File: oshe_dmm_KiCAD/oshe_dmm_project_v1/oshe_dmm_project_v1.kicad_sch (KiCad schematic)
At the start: 46 parts, among them J1 FTDI Basic, J2 USB_C_Receptacle_PowerOnly_6P, J3 Conn_01x02, SW1 SW_Push, U1 ATmega328P-A, U2 INA219BxD, U3 BQ24075RGT, U4 LM317_SOT-223, Y1 16MHz

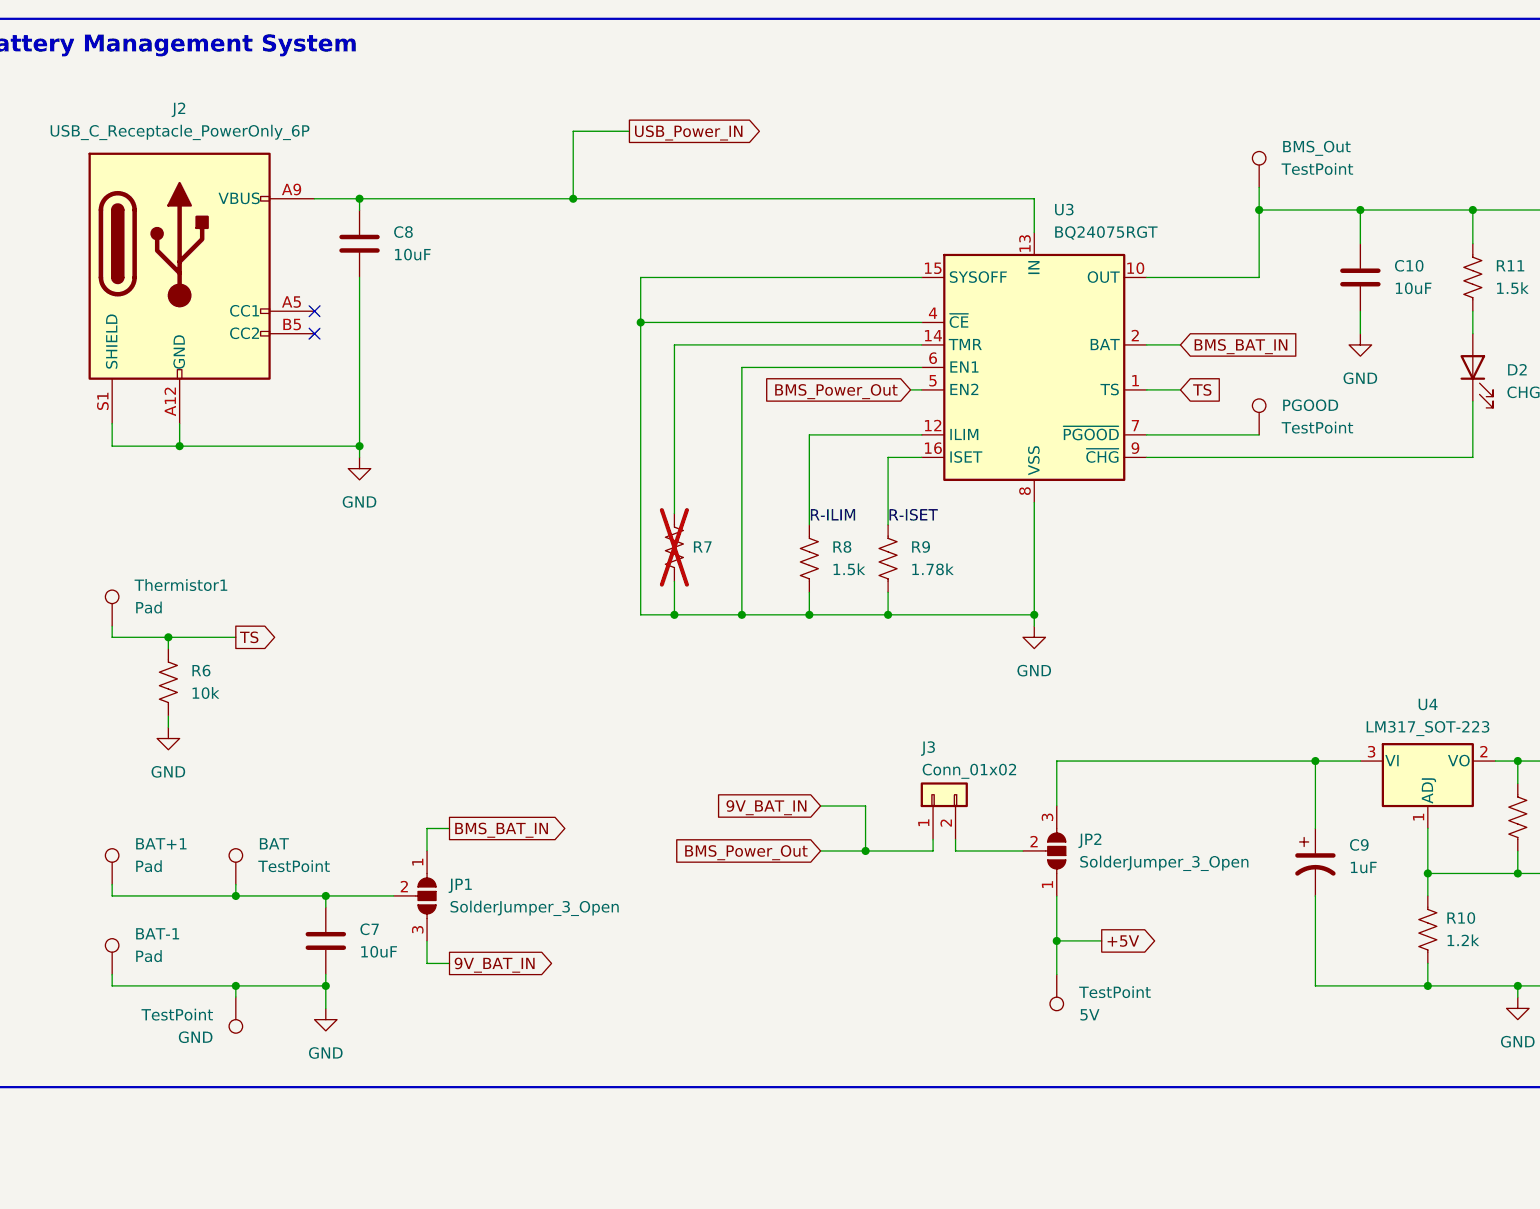
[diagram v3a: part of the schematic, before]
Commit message: Finalized the BMS system
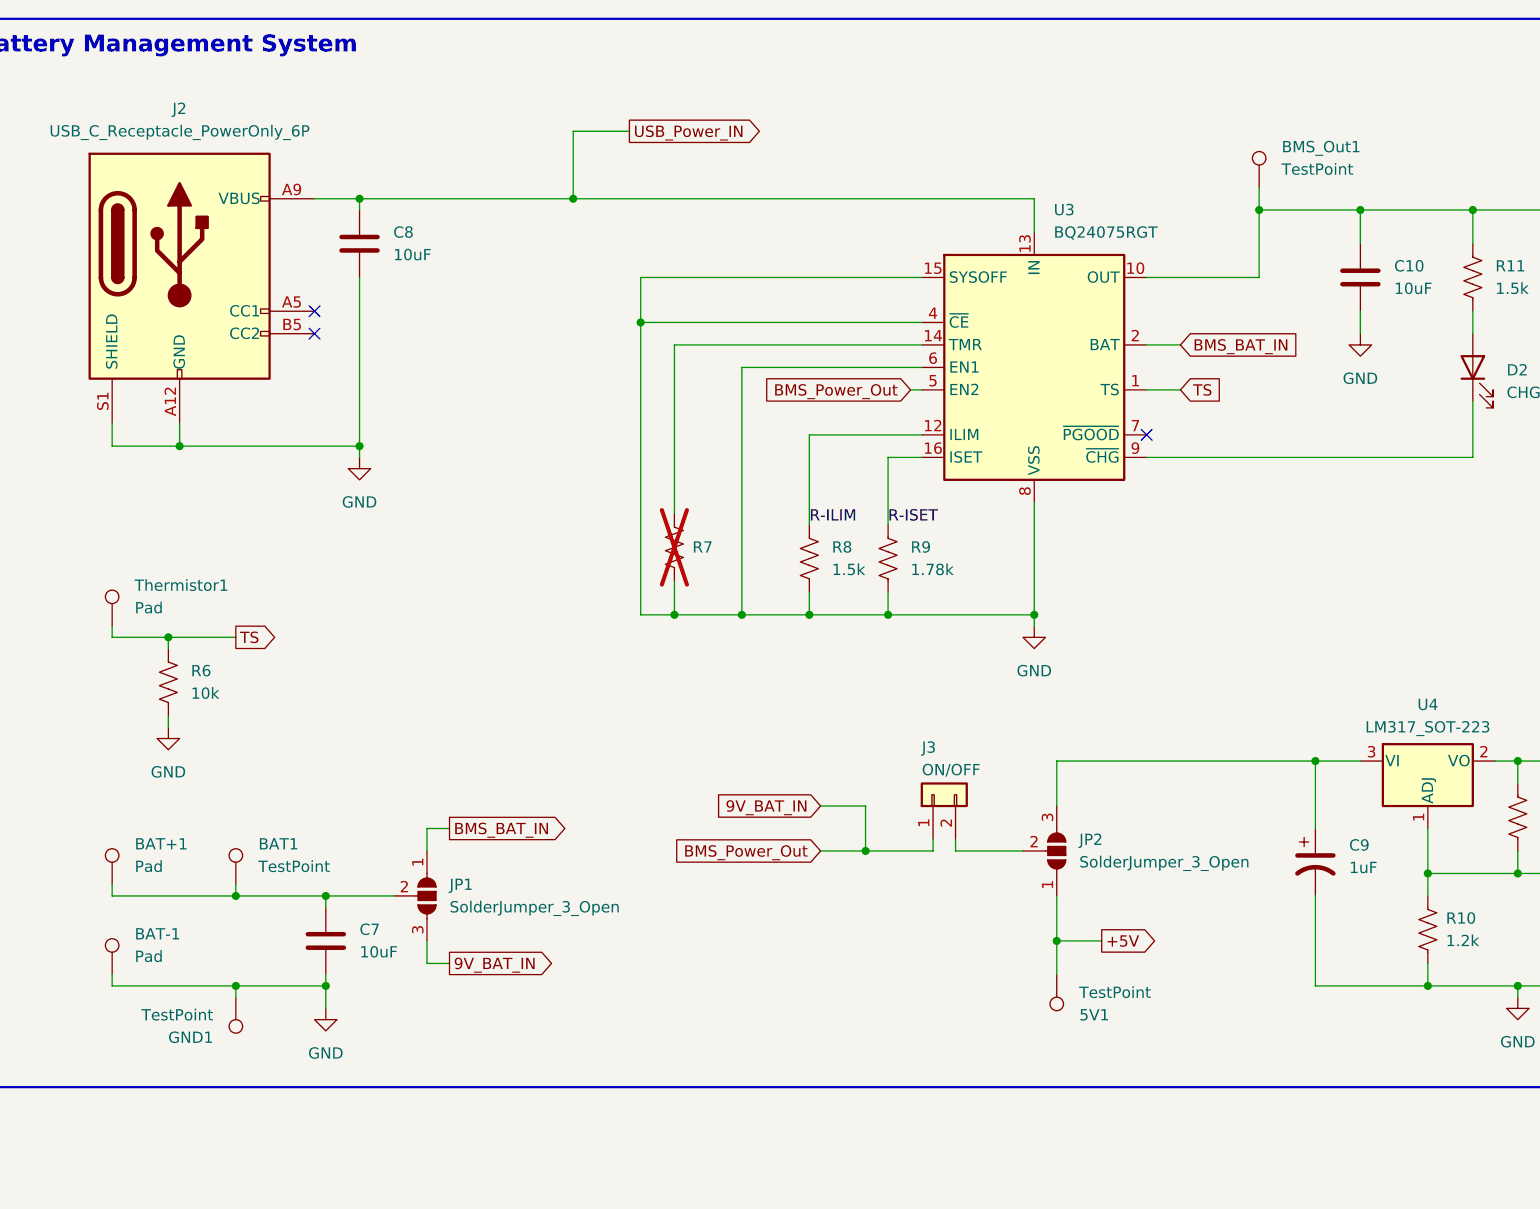
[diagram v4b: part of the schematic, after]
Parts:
- removed PGOOD: TestPoint, TestPoint:TestPoint_Keystone_5019_Minature, symbol Connector:TestPoint
- J3: value Conn_01x02 -> ON/OFF
- renumbered 5V to 5V1, BAT to BAT1, BMS_Out to BMS_Out1, GND to GND1
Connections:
- no-connect marks 2 -> 3
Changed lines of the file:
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@@
 	)
 	(no_connect
+		(at 490.22 63.5)
+	)
+	(no_connect
 		(at 396.24 52.07)
 	)
@@
 	(wire
 		(pts
-			(xy 490.22 63.5) (xy 502.92 63.5)
-		)
-		(stroke
-			(width 0)
-			(type default)
-		)
-	)
-	(wire
-		(pts
 			(xy 509.27 125.73) (xy 521.97 125.73)
 		)
@@
 		(dnp no)
 		(fields_autoplaced yes)
-		(property "Reference" "#PWR09"
+		(property "Reference" "#PWR011"
 			(at 401.32 72.39 0)
 			(effects
@@
 			(project "oshe_dmm_project_v1"
 				(path "/24c8480a-c336-4df0-8536-7016ee8fc0ac"
-					(reference "#PWR09")
+					(reference "#PWR011")
 					(unit 1)
 				)
@@
 		(on_board yes)
 		(dnp no)
-		(property "Reference" "BAT"
+		(property "Reference" "BAT1"
 			(at 389.89 109.7279 0)
 			(effects
@@
 			(project "oshe_dmm_project_v1"
 				(path "/24c8480a-c336-4df0-8536-7016ee8fc0ac"
-					(reference "BAT")
+					(reference "BAT1")
 					(unit 1)
 				)
@@
 		(on_board yes)
 		(dnp no)
-		(property "Reference" "5V"
+		(property "Reference" "5V1"
 			(at 482.6 129.0321 0)
 			(effects
@@
 			(project "oshe_dmm_project_v1"
 				(path "/24c8480a-c336-4df0-8536-7016ee8fc0ac"
-					(reference "5V")
+					(reference "5V1")
 					(unit 1)
 				)
@@
 		(dnp no)
 		(fields_autoplaced yes)
-		(property "Reference" "#PWR05"
+		(property "Reference" "#PWR07"
 			(at 111.76 72.39 0)
 			(effects
@@
 			(project ""
 				(path "/24c8480a-c336-4df0-8536-7016ee8fc0ac"
-					(reference "#PWR05")
+					(reference "#PWR07")
 					(unit 1)
 				)
@@
 		(dnp no)
 		(fields_autoplaced yes)
-		(property "Reference" "#PWR08"
+		(property "Reference" "#PWR010"
 			(at 397.51 134.62 0)
 			(effects
@@
 			(project "oshe_dmm_project_v1"
 				(path "/24c8480a-c336-4df0-8536-7016ee8fc0ac"
-					(reference "#PWR08")
+					(reference "#PWR010")
 					(unit 1)
 				)
@@
 		(dnp no)
 		(fields_autoplaced yes)
-		(property "Reference" "#PWR015"
+		(property "Reference" "#PWR04"
 			(at 67.31 180.34 0)
 			(effects
@@
 			(project "oshe_dmm_project_v1"
 				(path "/24c8480a-c336-4df0-8536-7016ee8fc0ac"
-					(reference "#PWR015")
+					(reference "#PWR04")
 					(unit 1)
 				)
@@
 	)
 	(symbol
-		(lib_id "Connector:TestPoint")
-		(at 502.92 63.5 0)
-		(unit 1)
-		(exclude_from_sim no)
-		(in_bom yes)
-		(on_board yes)
-		(dnp no)
-		(property "Reference" "PGOOD"
-			(at 505.46 60.198 0)
-			(effects
-				(font
-					(size 1.27 1.27)
-				)
-				(justify left)
-			)
-		)
-		(property "Value" "TestPoint"
-			(at 505.46 62.738 0)
-			(effects
-				(font
-					(size 1.27 1.27)
-				)
-				(justify left)
-			)
-		)
-		(property "Footprint" "TestPoint:TestPoint_Keystone_5019_Minature"
-			(at 508 63.5 0)
-			(effects
-				(font
-					(size 1.27 1.27)
-				)
-				(hide yes)
-			)
-		)
-		(property "Datasheet" "~"
-			(at 508 63.5 0)
-			(effects
-				(font
-					(size 1.27 1.27)
-				)
-				(hide yes)
-			)
-		)
-		(property "Description" "test point"
-			(at 502.92 63.5 0)
-			(effects
-				(font
-					(size 1.27 1.27)
-				)
-				(hide yes)
-			)
-		)
-		(pin "1"
-		)
-		(instances
-			(project ""
-				(path "/24c8480a-c336-4df0-8536-7016ee8fc0ac"
-					(reference "PGOOD")
-					(unit 1)
-				)
-			)
-		)
-	)
-	(symbol
 		(lib_id "Switch:SW_Push")
 		(at 90.17 86.36 90)
@@
 		(dnp no)
 		(fields_autoplaced yes)
-		(property "Reference" "#PWR010"
+		(property "Reference" "#PWR012"
 			(at 477.52 91.44 0)
 			(effects
@@
 			(project "oshe_dmm_project_v1"
 				(path "/24c8480a-c336-4df0-8536-7016ee8fc0ac"
-					(reference "#PWR010")
+					(reference "#PWR012")
 					(unit 1)
 				)
@@
 		(on_board yes)
 		(dnp no)
-		(property "Reference" "GND"
+		(property "Reference" "GND1"
 			(at 384.81 131.5721 0)
 			(effects
@@
 			(project "oshe_dmm_project_v1"
 				(path "/24c8480a-c336-4df0-8536-7016ee8fc0ac"
-					(reference "GND")
+					(reference "GND1")
 					(unit 1)
 				)
@@
 		(dnp no)
 		(fields_autoplaced yes)
-		(property "Reference" "#PWR03"
+		(property "Reference" "#PWR05"
 			(at 77.47 38.1 0)
 			(effects
@@
 			(project "oshe_dmm_project_v1"
 				(path "/24c8480a-c336-4df0-8536-7016ee8fc0ac"
-					(reference "#PWR03")
+					(reference "#PWR05")
 					(unit 1)
 				)
@@
 		(dnp no)
 		(fields_autoplaced yes)
-		(property "Reference" "#PWR04"
+		(property "Reference" "#PWR06"
 			(at 90.17 99.06 0)
 			(effects
@@
 			(project "oshe_dmm_project_v1"
 				(path "/24c8480a-c336-4df0-8536-7016ee8fc0ac"
-					(reference "#PWR04")
+					(reference "#PWR06")
 					(unit 1)
 				)
@@
 			)
 		)
-		(property "Value" "Conn_01x02"
+		(property "Value" "ON/OFF"
 			(at 464.82 101.346 90)
 			(effects
@@
 		(dnp no)
 		(fields_autoplaced yes)
-		(property "Reference" "#PWR07"
+		(property "Reference" "#PWR09"
 			(at 379.73 102.87 0)
 			(effects
@@
 			(project "oshe_dmm_project_v1"
 				(path "/24c8480a-c336-4df0-8536-7016ee8fc0ac"
-					(reference "#PWR07")
+					(reference "#PWR09")
 					(unit 1)
 				)
@@
 		(on_board yes)
 		(dnp no)
-		(property "Reference" "BMS_Out"
+		(property "Reference" "BMS_Out1"
 			(at 505.46 30.9879 0)
 			(effects
@@
 			(project "oshe_dmm_project_v1"
 				(path "/24c8480a-c336-4df0-8536-7016ee8fc0ac"
-					(reference "BMS_Out")
+					(reference "BMS_Out1")
 					(unit 1)
 				)
@@
 		(dnp no)
 		(fields_autoplaced yes)
-		(property "Reference" "#PWR02"
+		(property "Reference" "#PWR03"
 			(at 58.42 120.65 0)
 			(effects
@@
 			(project "oshe_dmm_project_v1"
 				(path "/24c8480a-c336-4df0-8536-7016ee8fc0ac"
-					(reference "#PWR02")
+					(reference "#PWR03")
 					(unit 1)
 				)
@@
 		(dnp no)
 		(fields_autoplaced yes)
-		(property "Reference" "#PWR06"
+		(property "Reference" "#PWR08"
 			(at 118.11 46.99 0)
 			(effects
@@
 			(project "oshe_dmm_project_v1"
 				(path "/24c8480a-c336-4df0-8536-7016ee8fc0ac"
-					(reference "#PWR06")
+					(reference "#PWR08")
 					(unit 1)
 				)
@@
 		(on_board yes)
 		(dnp no)
-		(property "Reference" "#PWR013"
+		(property "Reference" "#PWR02"
 			(at 53.34 152.4 0)
 			(effects
@@
 			(project "oshe_dmm_project_v1"
 				(path "/24c8480a-c336-4df0-8536-7016ee8fc0ac"
-					(reference "#PWR013")
+					(reference "#PWR02")
 					(unit 1)
 				)
@@
 		(dnp no)
 		(fields_autoplaced yes)
-		(property "Reference" "#PWR012"
+		(property "Reference" "#PWR014"
 			(at 532.13 133.35 0)
 			(effects
@@
 			(project "oshe_dmm_project_v1"
 				(path "/24c8480a-c336-4df0-8536-7016ee8fc0ac"
-					(reference "#PWR012")
+					(reference "#PWR014")
 					(unit 1)
 				)
@@
 		(dnp no)
 		(fields_autoplaced yes)
-		(property "Reference" "#PWR011"
+		(property "Reference" "#PWR013"
 			(at 514.35 58.42 0)
 			(effects
@@
 			(project "oshe_dmm_project_v1"
 				(path "/24c8480a-c336-4df0-8536-7016ee8fc0ac"
-					(reference "#PWR011")
+					(reference "#PWR013")
 					(unit 1)
 				)

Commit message: Made some PCB and Schematic Changes
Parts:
- added C4: 0.15 μf, oshe:CKG57K, symbol Device:C
- added COMin1, Vin1: ~, symbol oshe:Input
- added D1: SMAJ200CA, Diode_SMD:D_SMA, symbol Diode:SMAJ200CA
- added F1: Fuse, Fuse:Fuseholder_Clip-5x20mm_Keystone_3512P_Inline_P23.62x7.27mm_D1.02x2.41x1.02x1.57mm_Horizontal, symbol Device:Fuse
- added J4: Conn_01x16, Connector_PinSocket_2.54mm:PinSocket_1x16_P2.54mm_Vertical, symbol Connector_Generic:Conn_01x16
- added R1: R_US, Resistor_SMD:R_1206_3216Metric_Pad1.30x1.75mm_HandSolder, symbol Device:R_US
- added R15: 900K, symbol Device:R
- added R16: 90k, symbol Device:R
- added R17: 9k, symbol Device:R
- added R18: 1k, symbol Device:R
- added R4: 10k, Resistor_SMD:R_1206_3216Metric_Pad1.30x1.75mm_HandSolder, symbol Device:R_US
- added RV1: Varistor, symbol Device:Varistor
- added RV2: 10k, Potentiometer_SMD:Potentiometer_ACP_CA6-VSMD_Vertical, symbol Device:R_Potentiometer_US
- added SW2: SW_Rotary_1x4_MP, symbol Switch:SW_Rotary_1x4_MP
- added TP1: V-, symbol Connector:TestPoint_Probe
- added TP2: V+, symbol Connector:TestPoint_Probe
- added U5: ADS1115IDGS, Package_SO:TSSOP-10_3x3mm_P0.5mm, symbol Analog_ADC:ADS1115IDGS
- added Vout+1, Vout-1: ~, symbol oshe:Node
- JP1, JP2: value SolderJumper_3_Open -> SolderJumper
- renumbered C9 to C10, C10 to C11, C11 to C12, C12 to C13, C4 to C5, C5 to C6, C6 to C7, C7 to C8, C8 to C9, D1 to D2, D2 to D3, D3 to D4, R8 to R10, R9 to R11, R10 to R12, R11 to R13, R12 to R14, R1 to R2, R2 to R3, R3 to R5, R4 to R6, R5 to R7, R6 to R8, R7 to R9
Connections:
- net +5V: now also J4.15 (Pin_15), J4.2 (Pin_2), RV2.1
- net D2: now also J4.14 (Pin_14)
- net D3: now also J4.13 (Pin_13)
- net D4: now also J4.12 (Pin_12)
- net D5: now also J4.11 (Pin_11)
- net GND: now also J4.1 (Pin_1), J4.16 (Pin_16), J4.5 (Pin_5), RV2.2
- net MISO/D12: now also J4.6 (Pin_6)
- net MOSI/D11: now also J4.4 (Pin_4)
- new net: F1.1, Vin1.
- new net: F1.2, R1.1
- new net: D1.2 (A2), R1.2, R4.1
- new net: C4.1, R4.2, Vout+1.
- new net: C4.2, COMin1., D1.1 (A1), Vout-1.
- new net: SW2.5, U5.4 (AIN0)
- new net: J4.3 (Pin_3), RV2.3
- new net 200mv: R15.1, RV1.1, SW2.1, TP2.1
- new net 200v: R17.2, R18.1, SW2.4
- new net 20v: R16.2, R17.1, SW2.3
- new net 2v: R15.2, R16.1, SW2.2
- new net ground: R18.2, RV1.2, TP1.1, U5.3 (GND)
- no-connect marks 3 -> 7
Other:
- removed sheet Input_Protection
- removed sheet Voltage_Measurement
- note added: "Input Protection"
- note added: "LCD"
- note added: "Voltage Measurement (ADS1115)"
- moved on the sheet: 5V1, BAT+1, BAT-1, BAT1, BMS_Out1, C1, C10, C11, C12, C13, C2, C3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
